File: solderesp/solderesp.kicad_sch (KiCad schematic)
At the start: 1 part, among them U1 ESP32-WROOM-32

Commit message: Added Titles to SCH
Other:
- company: (none) -> avatarsd LLC
- title: (none) -> Solder Stantion Esphome
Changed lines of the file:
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@@
 	(generator_version "8.0")
 	(paper "A4")
+	(title_block
+		(title "Solder Stantion Esphome")
+		(date "2024-12-09")
+		(rev "a0")
+		(company "avatarsd LLC")
+		(comment 1 "by SD & MRK")
+	)
 	(symbol
 		(lib_id "RF_Module:ESP32-WROOM-32")

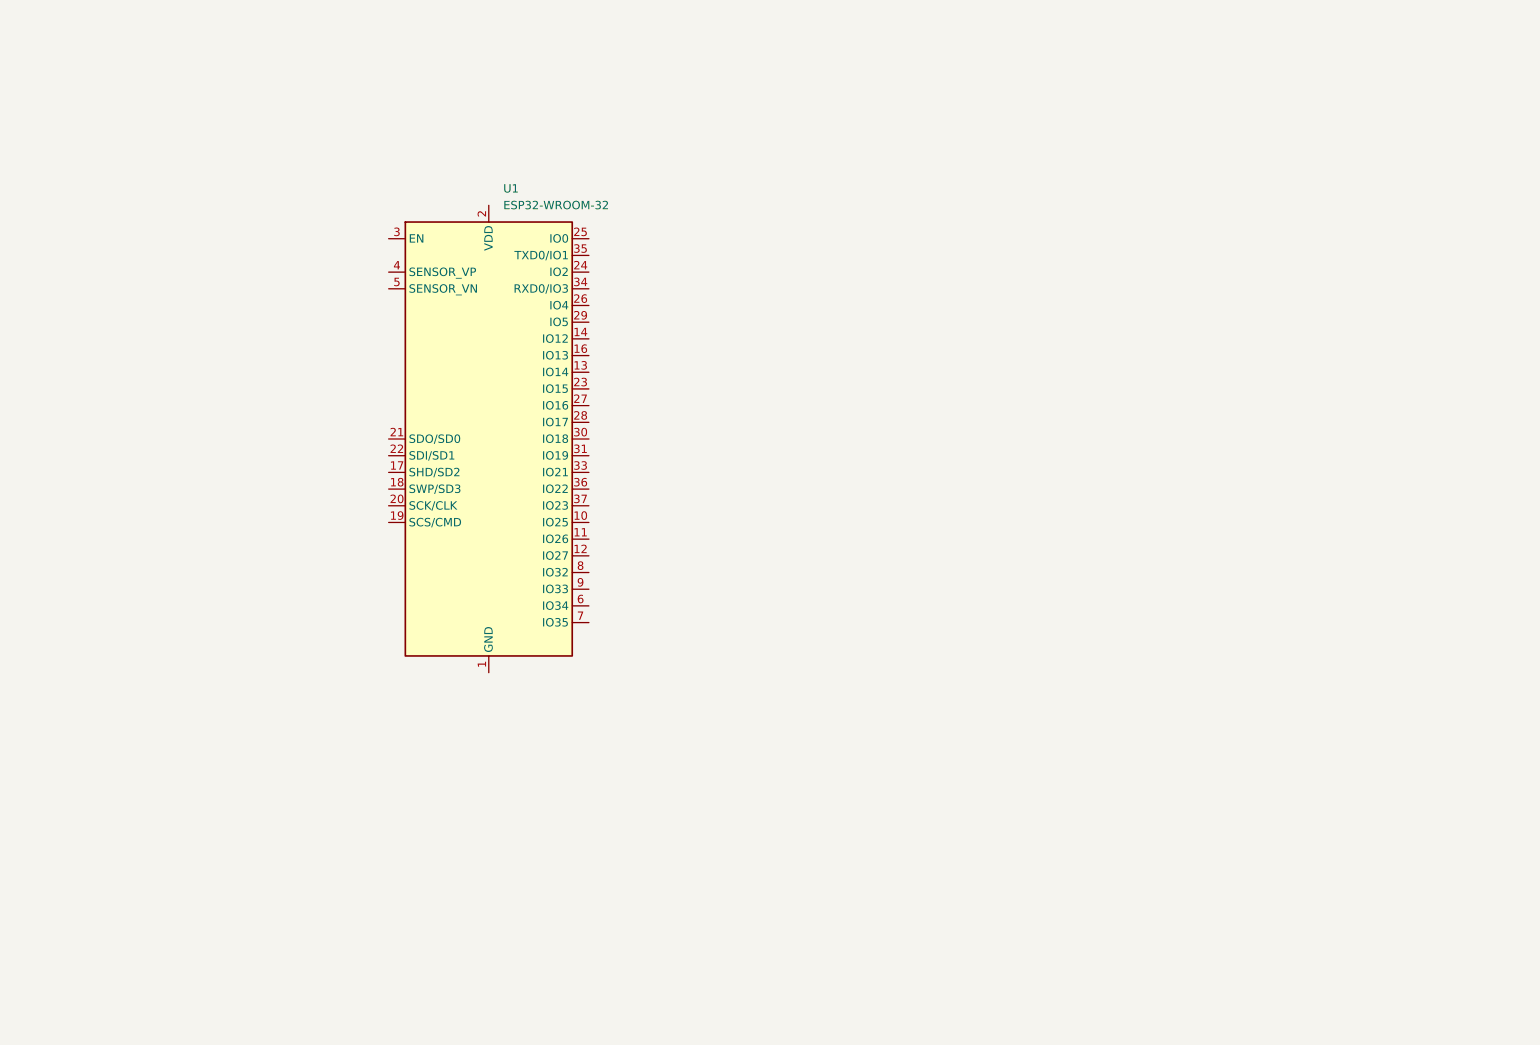
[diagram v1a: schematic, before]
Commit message: Imported Type-C PD trigger SCH
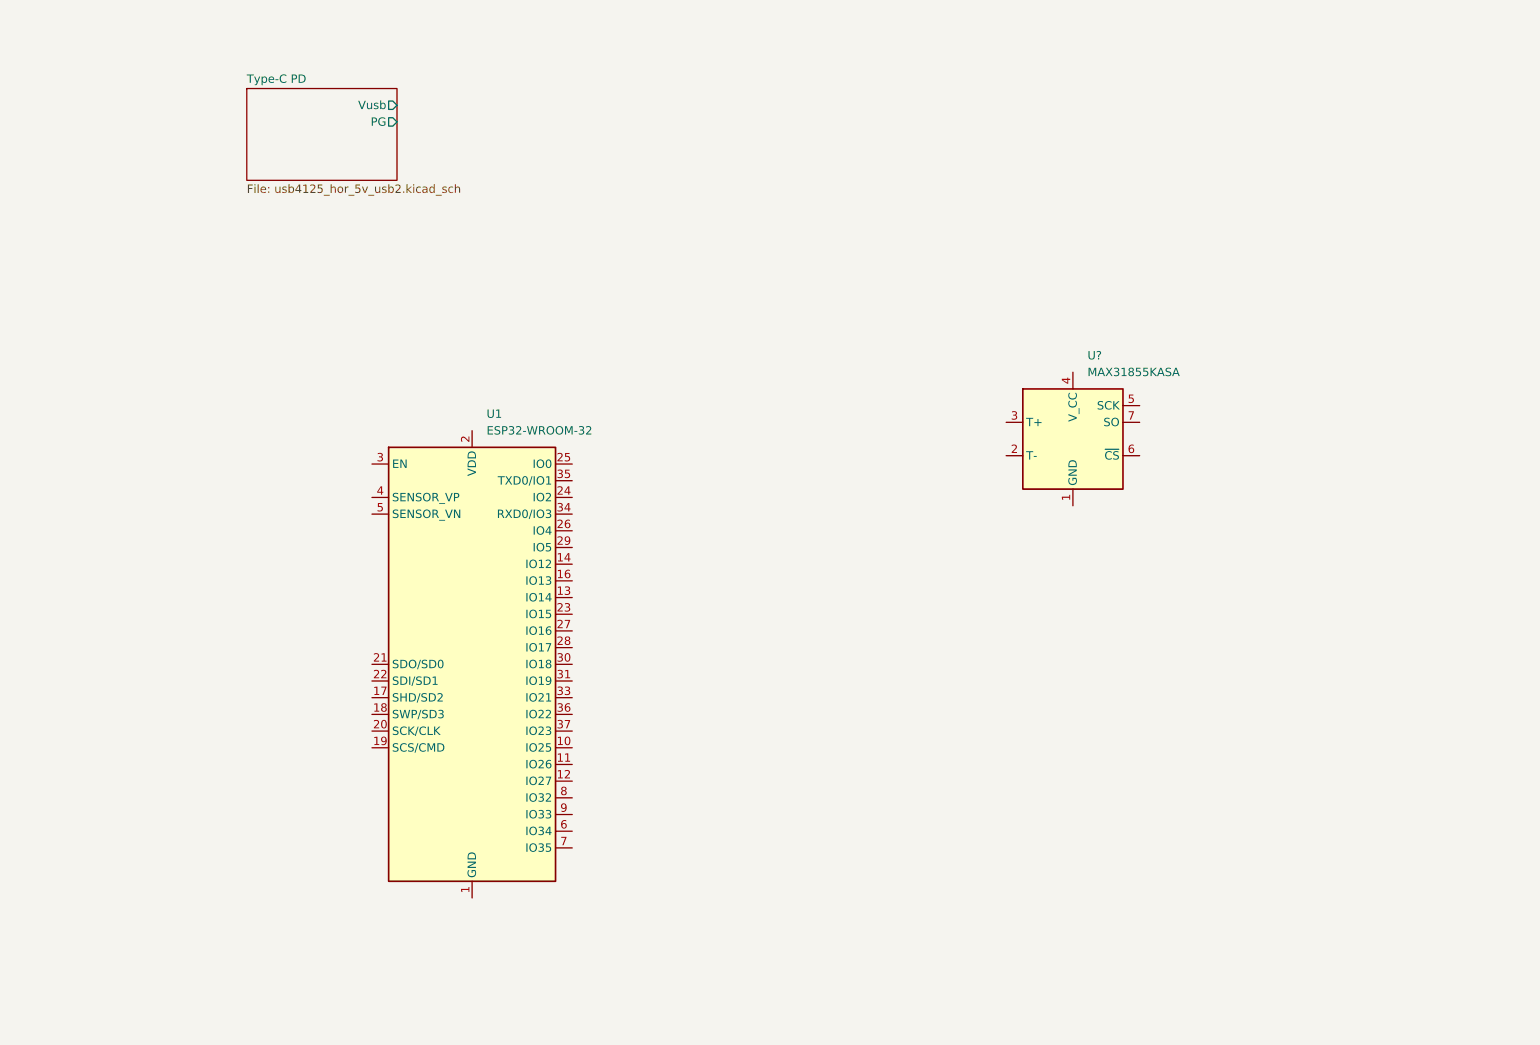
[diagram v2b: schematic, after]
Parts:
- added U?: MAX31855KASA, Package_SO:SOIC-8_3.9x4.9mm_P1.27mm, symbol Sensor_Temperature:MAX31855KASA
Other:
- added sheet Type-C PD (usb4125_hor_5v_usb2.kicad_sch)
- moved on the sheet: U1
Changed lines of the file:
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@@
+	)
+	(symbol
+		(lib_id "Sensor_Temperature:MAX31855KASA")
+		(at 191.77 83.82 0)
+		(unit 1)
+		(exclude_from_sim no)
+		(in_bom yes)
+		(on_board yes)
+		(dnp no)
+		(fields_autoplaced yes)
+		(property "Reference" "U?"
+			(at 193.9842 71.12 0)
+			(effects
+				(font
+					(size 1.27 1.27)
+				)
+				(justify left)
+			)
+		)
+		(property "Value" "MAX31855KASA"
+			(at 193.9842 73.66 0)
+			(effects
+				(font
+					(size 1.27 1.27)
+				)
+				(justify left)
+			)
+		)
+		(property "Footprint" "Package_SO:SOIC-8_3.9x4.9mm_P1.27mm"
+			(at 217.17 92.71 0)
+			(effects
+				(font
+					(size 1.27 1.27)
+					(italic yes)
+				)
+				(hide yes)
+			)
+		)
+		(property "Datasheet" "http://datasheets.maximintegrated.com/en/ds/MAX31855.pdf"
+			(at 191.77 83.82 0)
+			(effects
+				(font
+					(size 1.27 1.27)
+				)
+				(hide yes)
+			)
+		)
+		(property "Description" "Cold Junction K-type Termocouple Interface, SPI, SO8"
+			(at 191.77 83.82 0)
+			(effects
+				(font
+					(size 1.27 1.27)
+				)
+				(hide yes)
+			)
+		)
+		(pin "5"
+		)
+		(pin "1"
+		)
+		(pin "7"
+		)
+		(pin "3"
+		)
+		(pin "4"
+		)
+		(pin "6"
+		)
+		(pin "2"
+		)
+		(instances
+			(project ""
+				(path "/b3e652a1-72fc-4441-b72a-7f4fd6791c69"
+					(reference "U?")
+					(unit 1)
+				)
+			)
+		)
 	)
 	(symbol
 		(lib_id "RF_Module:ESP32-WROOM-32")
-		(at 102.87 83.82 0)
+		(at 100.33 118.11 0)
 		(unit 1)
 		(exclude_from_sim no)
@@
 		(fields_autoplaced yes)
 		(property "Reference" "U1"
-			(at 105.0641 45.72 0)
+			(at 102.5241 80.01 0)
 			(effects
 				(font
@@
 		)
 		(property "Value" "ESP32-WROOM-32"
-			(at 105.0641 48.26 0)
+			(at 102.5241 82.55 0)
 			(effects
 				(font
@@
 		)
 		(property "Footprint" "RF_Module:ESP32-WROOM-32"
-			(at 102.87 121.92 0)
+			(at 100.33 156.21 0)
 			(effects
 				(font
@@
 		)
 		(property "Datasheet" "https://www.espressif.com/sites/default/files/documentation/esp32-wroom-32_datasheet_en.pdf"
-			(at 95.25 82.55 0)
+			(at 92.71 116.84 0)
 			(effects
 				(font
@@
 		)
 		(property "Description" "RF Module, ESP32-D0WDQ6 SoC, Wi-Fi 802.11b/g/n, Bluetooth, BLE, 32-bit, 2.7-3.6V, onboard antenna, SMD"
-			(at 102.87 83.82 0)
+			(at 100.33 118.11 0)
 			(effects
 				(font
@@
 				)
 			)
+		)
+	)
+	(sheet
+		(at 66.04 30.48)
+		(size 22.86 13.97)
+		(fields_autoplaced yes)
+		(stroke
+			(width 0.1524)
+			(type solid)
+		)
+		(fill
+			(color 0 0 0 0.0000)
+		)
+		(property "Sheetname" "Type-C PD"
+			(at 66.04 29.7684 0)
+			(effects
+				(font
+					(size 1.27 1.27)
+				)
+				(justify left bottom)
+			)
+		)
+		(property "Sheetfile" "usb4125_hor_5v_usb2.kicad_sch"
+			(at 66.04 45.0346 0)
+			(effects
+				(font
+					(size 1.27 1.27)
+				)
+				(justify left top)
+			)
+		)
+		(pin "Vusb" output
+			(at 88.9 33.02 0)
+			(effects
+				(font
+					(size 1.27 1.27)
+				)
+				(justify right)
+			)
+		)
+		(pin "PG" output
+			(at 88.9 35.56 0)
+			(effects
+				(font
+					(size 1.27 1.27)
+				)
+				(justify right)
+			)
+		)
+		(instances
+			(project "solderesp"
+				(path "/b3e652a1-72fc-4441-b72a-7f4fd6791c69"
+					(page "2")
+				)
+			)

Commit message: Required symbols SCH & 3D has been added
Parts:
- added D?: SS58, PCM_Diode_SMD_AKL:D_SMC, symbol PCM_Diode_Schottky_AKL:SS58
- added J?: PINHD_2x2_Male, Connector_PinHeader_2.54mm:PinHeader_2x02_P2.54mm_Vertical, symbol PCM_SL_Pin_Headers:PINHD_2x2_Male
- added Q?: PSMN5R2-60YL, Package_TO_SOT_SMD:LFPAK56, symbol Transistor_FET:PSMN5R2-60YL
- added R? (x15): R_0603, PCM_Resistor_SMD_AKL:R_0603_1608Metric, symbol PCM_Resistor_AKL:R_0603
- added R? (x3): R_2512, PCM_Resistor_SMD_AKL:R_2512_6332Metric, symbol PCM_Resistor_AKL:R_2512
- added SW?: RotaryEncoder_Switch_MP, symbol Device:RotaryEncoder_Switch_MP
- added U? (x3): OP249GS, Package_SO:SOIC-8_3.9x4.9mm_P1.27mm, symbol Amplifier_Operational:OP249GS
- added U?: LM317AEMP, PCM_Package_TO_SOT_SMD_AKL:SOT-223-3_TabPin2, symbol PCM_Voltage_Regulator_AKL:LM317AEMP
- added U?: ~, symbol solder_sym:oled_ssd1306_128x64
- added U?: CP2102N-Axx-xQFN28, Package_DFN_QFN:QFN-28-1EP_5x5mm_P0.5mm_EP3.35x3.35mm, symbol Interface_USB:CP2102N-Axx-xQFN28
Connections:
- net GND: now reaches U?.1 (GND)
- net GND: now also U1.1 (GND), U1.15 (GND), U1.38 (GND), U1.39 (GND), R?.1, R?.2, R?.2, R?.2, SW?.C, SW?.MP, U?.1 (GND), U?.2 (V-), U?.29 (GND), U?.3 (GND)
- net at U?.2 (T-): now also J?.4
- net at U?.3 (T+): now also J?.2
- new net: Q?.4 (G), U?.5
- new net: D?.2 (A), J?.3, Q?.5 (D)
- new net: Q?.1 (S), Q?.2 (S), Q?.3 (S), R?.1, R?.1, R?.1, U?.1 (+)
- new net: R?.2, U?.8 (-)
- new net Type-C PD/Dn: U?.5 (D-)
- new net Type-C PD/Dp: U?.4 (D+)
- new net VS: D?.1 (K), J?.1
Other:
- sheet Type-C PD ports: added Dn, Dp; removed none
- moved on the sheet: U1, U?

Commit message: Basic schematic
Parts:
- added C? (x13): C_0402, PCM_Capacitor_SMD_AKL:C_0402_1005Metric, symbol PCM_Capacitor_AKL:C_0402
- added R? (x4): R_0603, PCM_Resistor_SMD_AKL:R_0603_1608Metric, symbol PCM_Resistor_AKL:R_0603
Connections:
- net GND: now also R?.1, R?.1, SW?.S2, U?.1, C?.2, C?.2, C?.2, C?.2, C?.2, C?.2, C?.2, C?.2, C?.2, C?.2, C?.2, C?.2
- net Type-C PD/PG: now also R?.2
- net VS: now also R?.2, U?.3 (IN), U?.6 (V+), C?.1, C?.1, C?.1
- net at U?.3 (+): now also U1.27 (IO16)
- net at U?.4 (-): now also R?.1, R?.2
- net VDD: now reaches U?.2 (OUT)
- net VDD: now also R?.2, R?.2, R?.2, R?.2, R?.2, U1.2 (VDD), U?.2 (VCC), U?.6 (VDD), C?.1, C?.1, C?.1, C?.1, R?.2, R?.2
- net at U?.3 (SCL): now also R?.1, U1.28 (IO17)
- net at U?.4 (SDA): now also R?.1, U1.30 (IO18)
- net at U?.5 (SCK): now also R?.2
- net at U?.6 (~{CS}): now also R?.2
- net at U?.7 (SO): now also R?.2
- net at Q?.1 (S), Q?.2 (S), Q?.3 (S)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: now also C?.1
- net at SW?.A: now also R?.1, U1.26 (IO4), C?.1
- net at SW?.B: now also R?.1, U1.29 (IO5), C?.1
- net at SW?.S1: now also U1.14 (IO12), C?.1, R?.1
- net at R?.1: now also R?.2, U?.8 (-), C?.2
- net at R?.2: now also R?.1, U?.7
- net at R?.2: now also R?.1, U1.9 (IO33), C?.1
- net at R?.1: now also U1.24 (IO2)
- net at R?.1: now also U1.23 (IO15)
- net at U1.13 (IO14): now also R?.1
- net at U1.16 (IO13): now also R?.1
- net at U1.3 (EN): now also C?.1, R?.1
- net at U1.34 (RXD0/IO3): now also R?.2
- net at U1.35 (TXD0/IO1): now also R?.2
- net at U1.8 (IO32): now also R?.2
- net at U?.25 (RXD): now also R?.1
- net at U?.26 (TXD): now also R?.1
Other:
- moved on the sheet: R?, U?, U?C
